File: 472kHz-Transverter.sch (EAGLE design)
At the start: 92 parts, among them K1 CT112, K2 CT112, K3 CT112, Q1 3.072MHz, T1 2N3904, T2 2N3904, T3 2N3904, T4 2N3904, T5 2N3904, T6 BD436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

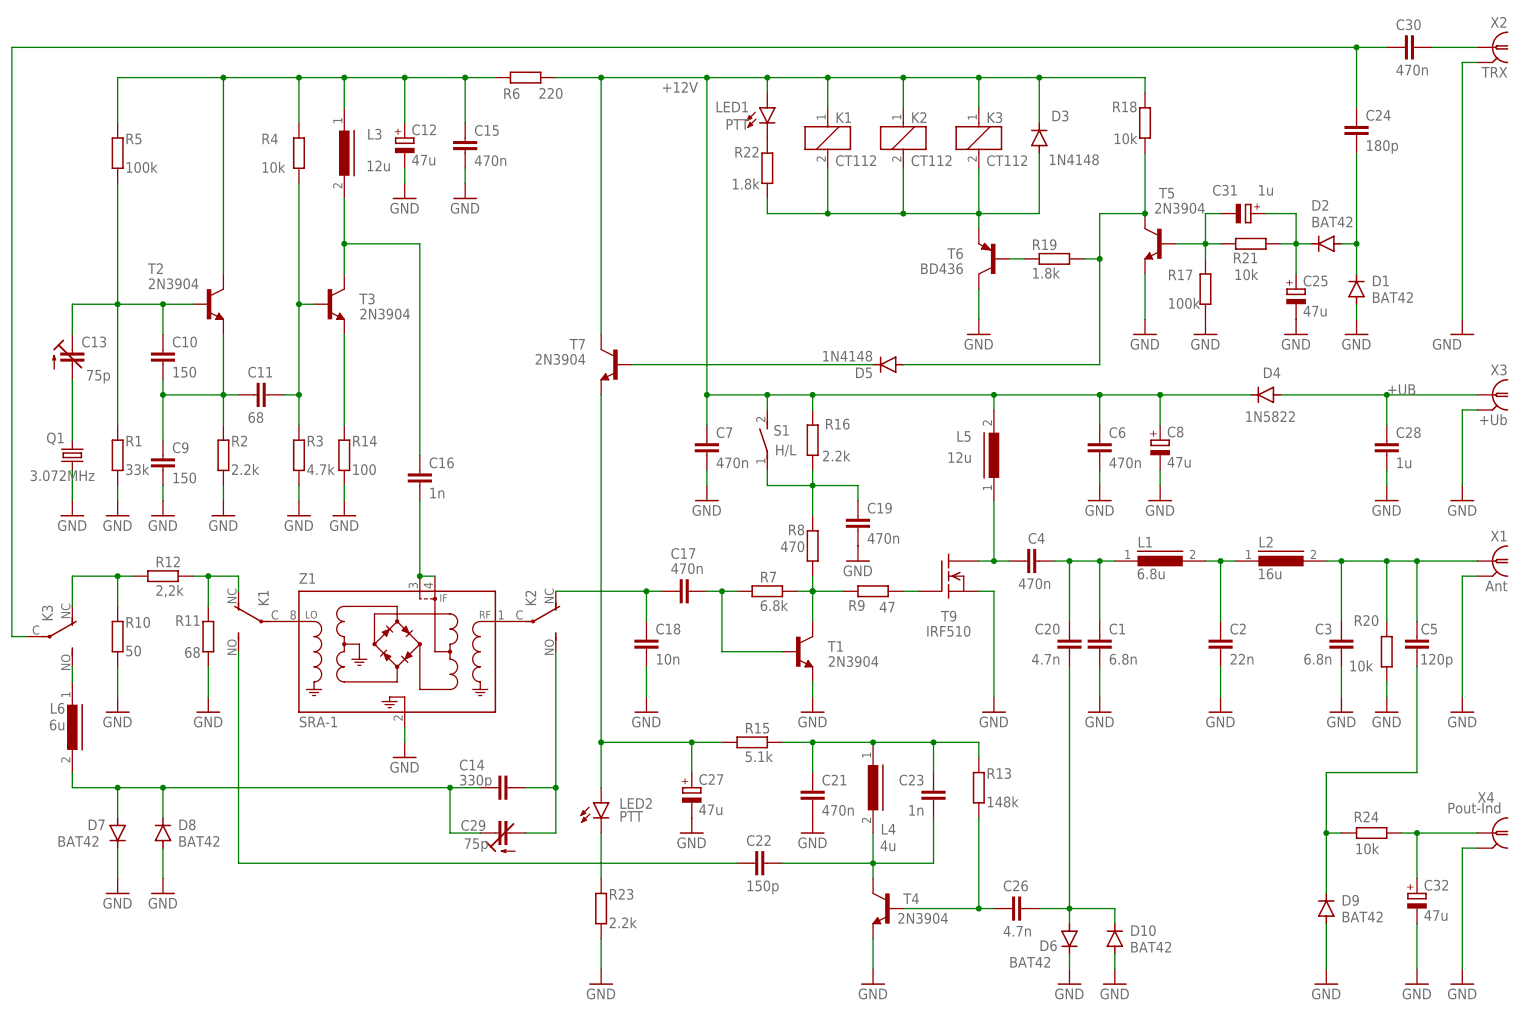
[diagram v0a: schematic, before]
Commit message: SRA-1 connections corrected
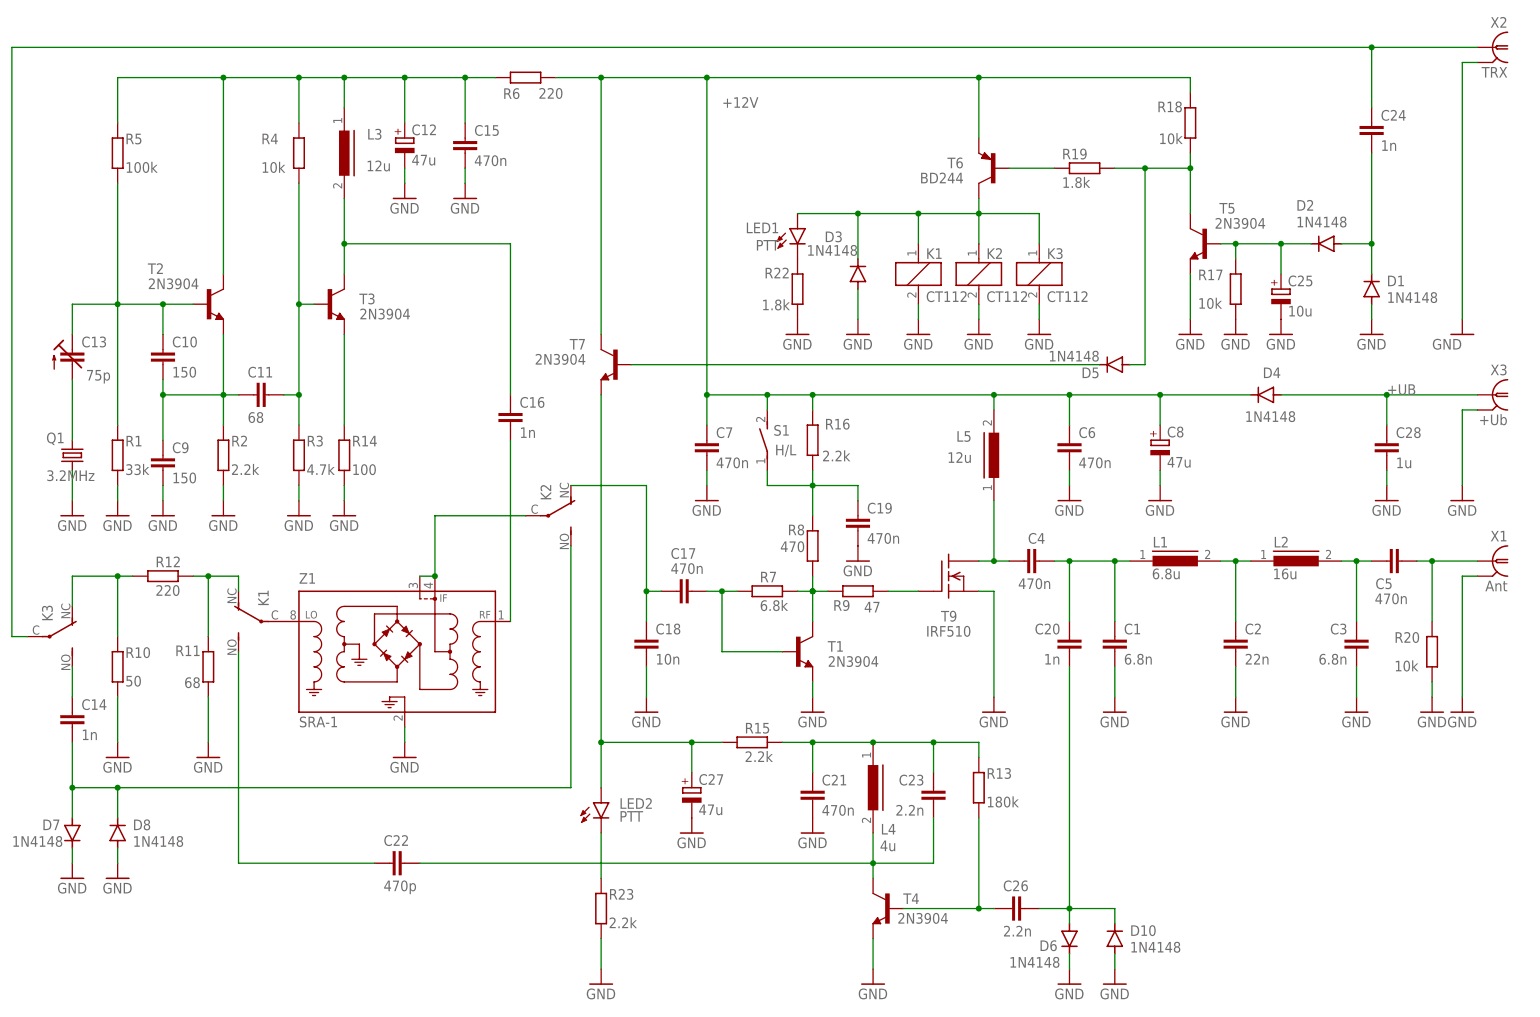
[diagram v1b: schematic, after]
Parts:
- removed C29: 75p, rcl:C-TRIMM808-1
- removed C30: 470n, capacitor-wima:C5/2.5
- removed C31: 1u, rcl:CPOL-EUCT7343
- removed C32: 47u, rcl:CPOL-EUCT7343
- removed D9: BAT42, diode:1N4148DO35-7
- removed L6: 6u, inductors:ED22
- removed R21, R24: 10k, rcl:R-EU_0207/5V
- removed X4: Pout-Ind, con-coax:R141426
- C14: value 330p -> 1n
- C20: value 4.7n -> 1n
- C22: value 150p -> 470p
- C23: value 1n -> 2.2n
- C24: value 180p -> 1n
- C25: value 47u -> 10u
- C26: value 4.7n -> 2.2n
- C5: value 120p -> 470n
- D1, D10, D2, D6, D7, D8: value BAT42 -> 1N4148
- D4: value 1N5822 -> 1N4148
- Q1: value 3.072MHz -> 3.2MHz
- R12: value 2,2k -> 220
- R13: value 148k -> 180k
- R15: value 5.1k -> 2.2k
- R17: value 100k -> 10k
- T6: value BD436 -> BD244
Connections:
- removed net N$10 (its old number): C32.+, R24.1, X4.1
- removed net N$33: C31.-, R17.2, R21.2, T5.B
- removed net N$35: C30.2, X2.1
- removed net N$38: C14.2, C29.A, K22.S
- removed net N$41: D3.A, K11.2, K21.2, K31.2, R22.1, T6.E
- new net N$29: D3.C, K11.1, K21.1, K31.1, LED1.A, T6.C
- net +12V: now also T6.E; no longer D3.C, K11.1, K21.1, K31.1, LED1.A
- net GND: now also D3.A, K11.2, K21.2, K31.2, R22.1; no longer C32.-, D9.A, T6.C, X4.2
- net N$1: now also C14.1; no longer L6.1
- net N$19: now also C16.2; no longer K22.P
- net N$20: now also K22.P; no longer C16.2
- net N$25: now also X2.1; no longer C30.1
- net N$3: no longer R20.2, X1.1
- net N$30: now also C14.2, K22.S; no longer C14.1, C29.E, L6.2
- net N$37: now also R17.2, T5.B; no longer C31.+, R21.1
- net N$5: now also R20.2, X1.1; no longer D9.C, R24.2
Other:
- moved on the sheet: C1, C14, C16, C2, C22, C24, C25, C3, C5, C6, D1, D3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
